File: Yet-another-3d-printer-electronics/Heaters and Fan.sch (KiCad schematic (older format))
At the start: 54 parts, among them P15 HEATER_BED, P16 HEATER_EXT, P18 FAN, P22 FAN, P23 HEATER_EXT, P4 FAN, Q1 2N7000, Q2 IRLR8743PBF, Q3 IRLML0030TRPBF, Q4 IRLR8743PBF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

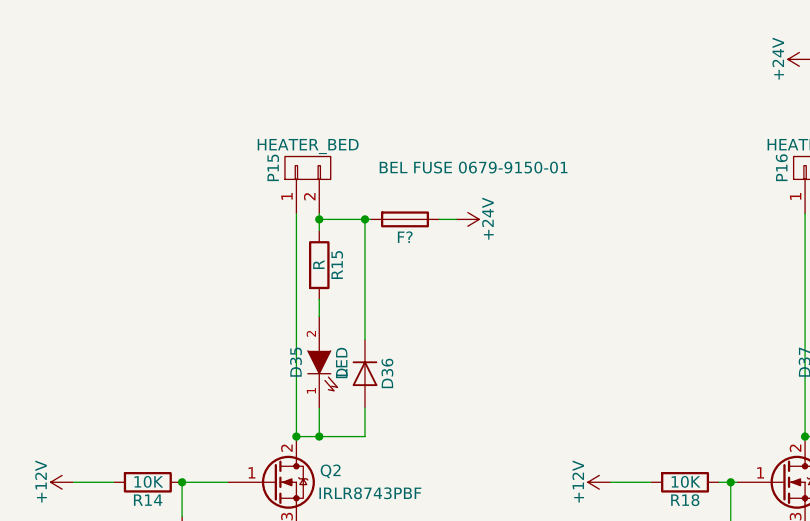
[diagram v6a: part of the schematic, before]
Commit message: Add programming jumper
Signed-off-by: Mateusz Krawczuk <mat.krawczuk@gmail.com>
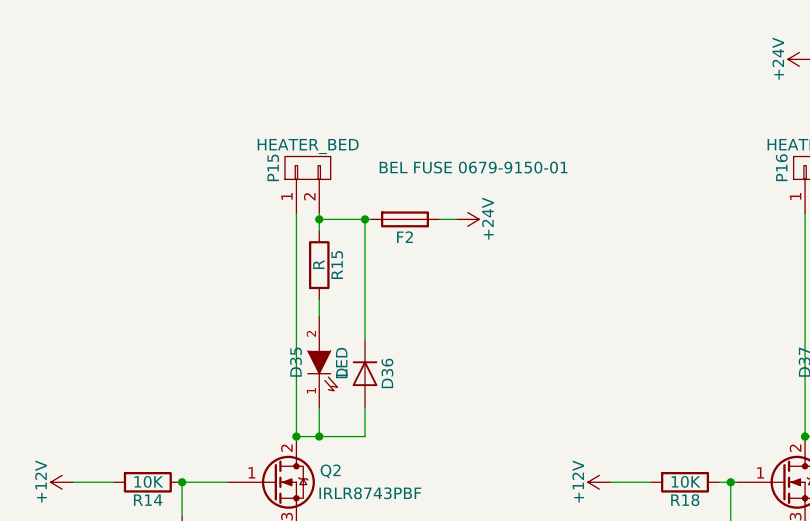
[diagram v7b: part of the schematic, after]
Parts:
- gave numbers to parts that had none: 1
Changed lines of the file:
@@
 $EndComp
 $Comp
-L GND #PWR0106
+L GND #PWR108
 U 1 1 58B2B47D
 P 2500 3325
-F 0 "#PWR0106" H 2500 3075 50  0001 C CNN
+F 0 "#PWR108" H 2500 3075 50  0001 C CNN
 F 1 "GND" H 2500 3175 50  0000 C CNN
 F 2 "" H 2500 3325 50  0000 C CNN
@@
 $EndComp
 $Comp
-L +24V #PWR0107
+L +24V #PWR109
 U 1 1 58B2B483
 P 3200 1850
-F 0 "#PWR0107" H 3200 1700 50  0001 C CNN
+F 0 "#PWR109" H 3200 1700 50  0001 C CNN
 F 1 "+24V" H 3200 1990 50  0000 C CNN
 F 2 "" H 3200 1850 50  0000 C CNN
@@
 $EndComp
 $Comp
-L GND #PWR0108
+L GND #PWR106
 U 1 1 58B2B497
 P 2000 3675
-F 0 "#PWR0108" H 2000 3425 50  0001 C CNN
+F 0 "#PWR106" H 2000 3425 50  0001 C CNN
 F 1 "GND" H 2000 3525 50  0000 C CNN
 F 2 "" H 2000 3675 50  0000 C CNN
@@
 $EndComp
 $Comp
-L GND #PWR0109
+L GND #PWR117
 U 1 1 58B2B4D4
 P 4725 3250
-F 0 "#PWR0109" H 4725 3000 50  0001 C CNN
+F 0 "#PWR117" H 4725 3000 50  0001 C CNN
 F 1 "GND" H 4725 3100 50  0000 C CNN
 F 2 "" H 4725 3250 50  0000 C CNN
@@
 $EndComp
 $Comp
-L GND #PWR0110
+L GND #PWR104
 U 1 1 58B2B4FD
 P 1675 6875
-F 0 "#PWR0110" H 1675 6625 50  0001 C CNN
+F 0 "#PWR104" H 1675 6625 50  0001 C CNN
 F 1 "GND" H 1675 6725 50  0000 C CNN
 F 2 "" H 1675 6875 50  0000 C CNN
@@
 $EndComp
 $Comp
-L +24V #PWR0111
+L +24V #PWR105
 U 1 1 58B2B503
 P 1700 4700
-F 0 "#PWR0111" H 1700 4550 50  0001 C CNN
+F 0 "#PWR105" H 1700 4550 50  0001 C CNN
 F 1 "+24V" H 1700 4840 50  0000 C CNN
 F 2 "" H 1700 4700 50  0000 C CNN
@@
 $EndComp
 $Comp
-L GND #PWR0112
+L GND #PWR115
 U 1 1 58B2B53B
 P 4400 3825
-F 0 "#PWR0112" H 4400 3575 50  0001 C CNN
+F 0 "#PWR115" H 4400 3575 50  0001 C CNN
 F 1 "GND" H 4400 3675 50  0000 C CNN
 F 2 "" H 4400 3825 50  0000 C CNN
@@
 $EndComp
 $Comp
-L +12V #PWR0113
+L +12V #PWR107
 U 1 1 58B0BD25
 P 2250 4700
-F 0 "#PWR0113" H 2250 4550 50  0001 C CNN
+F 0 "#PWR107" H 2250 4550 50  0001 C CNN
 F 1 "+12V" H 2250 4840 50  0000 C CNN
 F 2 "" H 2250 4700 50  0000 C CNN
@@
 $EndComp
 $Comp
-L +24V #PWR0114
+L +24V #PWR118
 U 1 1 58B0BF44
 P 4750 1150
-F 0 "#PWR0114" H 4750 1000 50  0001 C CNN
+F 0 "#PWR118" H 4750 1000 50  0001 C CNN
 F 1 "+24V" H 4750 1290 50  0000 C CNN
 F 2 "" H 4750 1150 50  0000 C CNN
@@
 $EndComp
 $Comp
-L +12V #PWR0115
+L +12V #PWR119
 U 1 1 58B0BF53
 P 5300 1150
-F 0 "#PWR0115" H 5300 1000 50  0001 C CNN
+F 0 "#PWR119" H 5300 1000 50  0001 C CNN
 F 1 "+12V" H 5300 1290 50  0000 C CNN
 F 2 "" H 5300 1150 50  0000 C CNN
@@
 	1775 5400 1975 5400
 $Comp
-L +12V #PWR0116
+L +12V #PWR113
 U 1 1 58B2884F
 P 3875 3000
-F 0 "#PWR0116" H 3875 2850 50  0001 C CNN
+F 0 "#PWR113" H 3875 2850 50  0001 C CNN
 F 1 "+12V" H 3875 3140 50  0000 C CNN
 F 2 "" H 3875 3000 50  0000 C CNN
@@
 $EndComp
 $Comp
-L +12V #PWR0117
+L +12V #PWR103
 U 1 1 58B28D51
 P 1525 3000
-F 0 "#PWR0117" H 1525 2850 50  0001 C CNN
+F 0 "#PWR103" H 1525 2850 50  0001 C CNN
 F 1 "+12V" H 1525 3140 50  0000 C CNN
 F 2 "" H 1525 3000 50  0000 C CNN
@@
 $EndComp
 $Comp
-L GND #PWR0118
+L GND #PWR111
 U 1 1 58FEC38F
 P 3725 6875
-F 0 "#PWR0118" H 3725 6625 50  0001 C CNN
+F 0 "#PWR111" H 3725 6625 50  0001 C CNN
 F 1 "GND" H 3725 6725 50  0000 C CNN
 F 2 "" H 3725 6875 50  0000 C CNN
@@
 $EndComp
 $Comp
-L +24V #PWR0119
+L +24V #PWR112
 U 1 1 58FEC395
 P 3750 4700
-F 0 "#PWR0119" H 3750 4550 50  0001 C CNN
+F 0 "#PWR112" H 3750 4550 50  0001 C CNN
 F 1 "+24V" H 3750 4840 50  0000 C CNN
 F 2 "" H 3750 4700 50  0000 C CNN
@@
 $EndComp
 $Comp
-L +12V #PWR0120
+L +12V #PWR114
 U 1 1 58FEC3C0
 P 4300 4700
-F 0 "#PWR0120" H 4300 4550 50  0001 C CNN
+F 0 "#PWR114" H 4300 4550 50  0001 C CNN
 F 1 "+12V" H 4300 4840 50  0000 C CNN
 F 2 "" H 4300 4700 50  0000 C CNN
@@
 	3825 5400 4025 5400
 $Comp
-L +5V #PWR0121
+L +5V #PWR102
 U 1 1 5900C78C
 P 1225 3725
-F 0 "#PWR0121" H 1225 3575 50  0001 C CNN
+F 0 "#PWR102" H 1225 3575 50  0001 C CNN
 F 1 "+5V" H 1225 3865 50  0000 C CNN
 F 2 "" H 1225 3725 50  0001 C CNN
@@
 $EndComp
 $Comp
-L +5V #PWR0122
+L +5V #PWR110
 U 1 1 5900D640
 P 3625 3850
-F 0 "#PWR0122" H 3625 3700 50  0001 C CNN
+F 0 "#PWR110" H 3625 3700 50  0001 C CNN
 F 1 "+5V" H 3625 3990 50  0000 C CNN
 F 2 "" H 3625 3850 50  0001 C CNN
@@
 $EndComp
 $Comp
-L +12V #PWR0123
+L +12V #PWR116
 U 1 1 59029923
 P 4400 4700
-F 0 "#PWR0123" H 4400 4550 50  0001 C CNN
+F 0 "#PWR116" H 4400 4550 50  0001 C CNN
 F 1 "+12V" H 4400 4840 50  0000 C CNN
 F 2 "" H 4400 4700 50  0000 C CNN
@@
 $EndComp
 $Comp
-L GND #PWR0124
+L GND #PWR120
 U 1 1 59029935
 P 5875 6875
-F 0 "#PWR0124" H 5875 6625 50  0001 C CNN
+F 0 "#PWR120" H 5875 6625 50  0001 C CNN
 F 1 "GND" H 5875 6725 50  0000 C CNN
 F 2 "" H 5875 6875 50  0000 C CNN
@@
 $EndComp
 $Comp
-L +24V #PWR0125
+L +24V #PWR121
 U 1 1 5902993B
 P 5900 4700
-F 0 "#PWR0125" H 5900 4550 50  0001 C CNN
+F 0 "#PWR121" H 5900 4550 50  0001 C CNN
 F 1 "+24V" H 5900 4840 50  0000 C CNN
 F 2 "" H 5900 4700 50  0000 C CNN
@@
 $EndComp
 $Comp
-L +12V #PWR0126
+L +12V #PWR123
 U 1 1 59029966
 P 6450 4700
-F 0 "#PWR0126" H 6450 4550 50  0001 C CNN
+F 0 "#PWR123" H 6450 4550 50  0001 C CNN
 F 1 "+12V" H 6450 4840 50  0000 C CNN
 F 2 "" H 6450 4700 50  0000 C CNN
@@
 $EndComp
 $Comp
-L GND #PWR0127
+L GND #PWR126
 U 1 1 5902A5C2
 P 7350 3275
-F 0 "#PWR0127" H 7350 3025 50  0001 C CNN
+F 0 "#PWR126" H 7350 3025 50  0001 C CNN
 F 1 "GND" H 7350 3125 50  0000 C CNN
 F 2 "" H 7350 3275 50  0000 C CNN
@@
 $EndComp
 $Comp
-L GND #PWR0128
+L GND #PWR125
 U 1 1 5902A5DA
 P 7025 3850
-F 0 "#PWR0128" H 7025 3600 50  0001 C CNN
+F 0 "#PWR125" H 7025 3600 50  0001 C CNN
 F 1 "GND" H 7025 3700 50  0000 C CNN
 F 2 "" H 7025 3850 50  0000 C CNN
@@
 HEAT_EXT2
 $Comp
-L +24V #PWR0129
+L +24V #PWR127
 U 1 1 5902A5F3
 P 7375 1175
-F 0 "#PWR0129" H 7375 1025 50  0001 C CNN
+F 0 "#PWR127" H 7375 1025 50  0001 C CNN
 F 1 "+24V" H 7375 1315 50  0000 C CNN
 F 2 "" H 7375 1175 50  0000 C CNN
@@
 $EndComp
 $Comp
-L +12V #PWR0130
+L +12V #PWR128
 U 1 1 5902A5FF
 P 7925 1175
-F 0 "#PWR0130" H 7925 1025 50  0001 C CNN
+F 0 "#PWR128" H 7925 1025 50  0001 C CNN
 F 1 "+12V" H 7925 1315 50  0000 C CNN
 F 2 "" H 7925 1175 50  0000 C CNN
@@
 Connection ~ 7650 1875
 $Comp
-L +12V #PWR0131
+L +12V #PWR124
 U 1 1 5902A61C
 P 6500 3025
-F 0 "#PWR0131" H 6500 2875 50  0001 C CNN
+F 0 "#PWR124" H 6500 2875 50  0001 C CNN
 F 1 "+12V" H 6500 3165 50  0000 C CNN
 F 2 "" H 6500 3025 50  0000 C CNN
@@
 	7650 1875 7450 1875
 $Comp
-L +5V #PWR0132
+L +5V #PWR122
 U 1 1 5902A623
 P 6250 3875
-F 0 "#PWR0132" H 6250 3725 50  0001 C CNN
+F 0 "#PWR122" H 6250 3725 50  0001 C CNN
 F 1 "+5V" H 6250 4015 50  0000 C CNN
 F 2 "" H 6250 3875 50  0001 C CNN
@@
 $EndComp
 $Comp
-L Fuse F?
+L Fuse F2
 U 1 1 5903EAF9
 P 2975 1850
-F 0 "F?" V 3055 1850 50  0000 C CNN
+F 0 "F2" V 3055 1850 50  0000 C CNN
 F 1 "BEL FUSE 0679-9150-01" V 2750 2150 50  0000 C CNN
 F 2 "" V 2905 1850 50  0001 C CNN

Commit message: Choose footprints for some components
Signed-off-by: Mateusz Krawczuk <mat.krawczuk@gmail.com>
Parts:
- R12, R13, R14, R16, R17, R18, R20, R21, R22, R24, R37, R38, R40, R41, R42: footprint Resistors_SMD:R_0805_HandSoldering -> Resistors_SMD:R_1206_HandSoldering
- R15, R19, R23, R25, R39, R43: footprint Resistors_SMD:R_0805_HandSoldering -> Resistors_SMD:R_2010_HandSoldering
